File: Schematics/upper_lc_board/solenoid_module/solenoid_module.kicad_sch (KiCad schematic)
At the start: 10 parts, among them J1 SOL_CONN, K1 RELAY_G5Q-1A, Q1 MOSFET_IRLZ44N

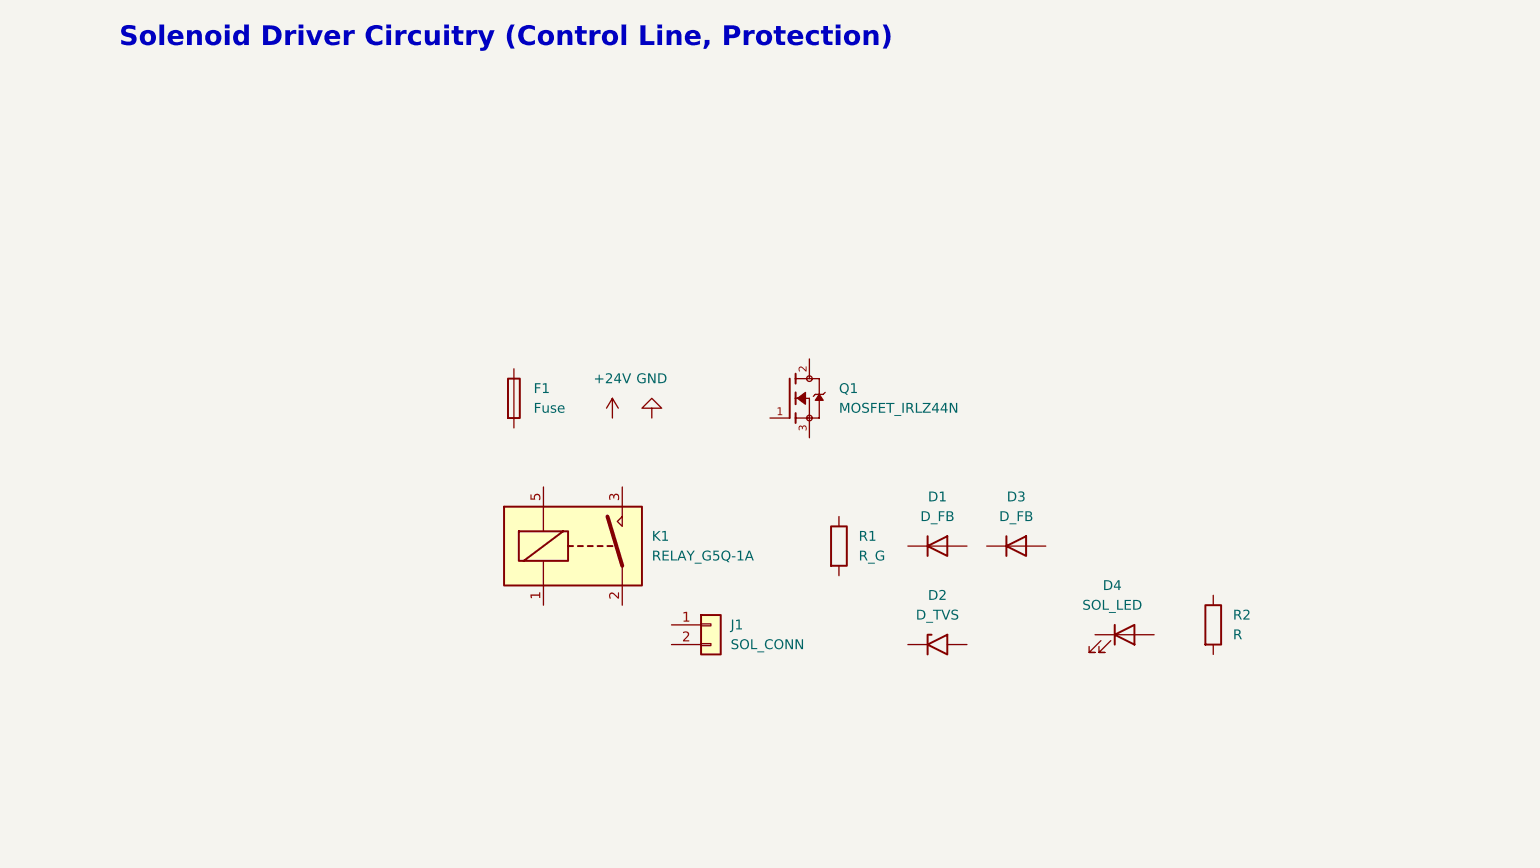
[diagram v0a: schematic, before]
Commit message: add solenoid driver circuitry
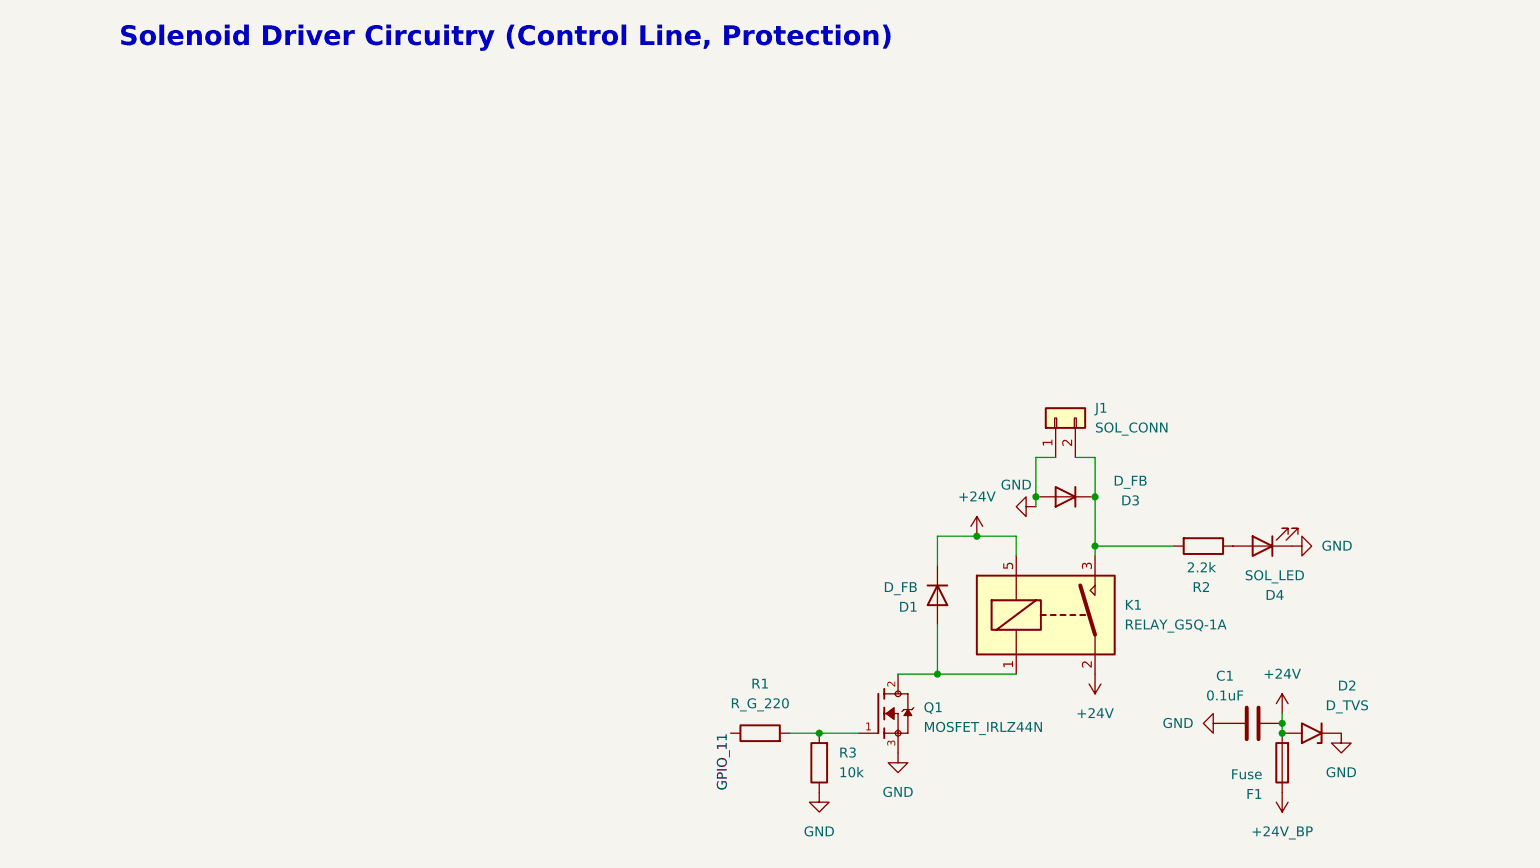
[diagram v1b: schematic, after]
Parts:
- added C1: 0.1uF, symbol Device:C
- added R3: 10k, symbol Device:R
- R1: value R_G -> R_G_220
- R2: value R -> 2.2k
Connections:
- net +24V: now also D1.1 (K), D2.2 (A2), F1.2, K1.2, K1.5, C1.2
- net GND: now also D2.1 (A1), D3.2 (A), D4.1 (K), J1.1 (Pin_1), Q1.3, C1.1, R3.1
- net GPIO_11: now reaches R1.1
- net at R1.2: now also Q1.1, R3.2
- net +24V_BP: now reaches F1.1
- net at R2.1: now also D4.2 (A)
- net at R2.2: now also D3.1 (K), J1.2 (Pin_2), K1.3
- net at D1.2 (A): now also K1.1, Q1.2
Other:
- moved on the sheet: F1, J1, K1, Q1, R1

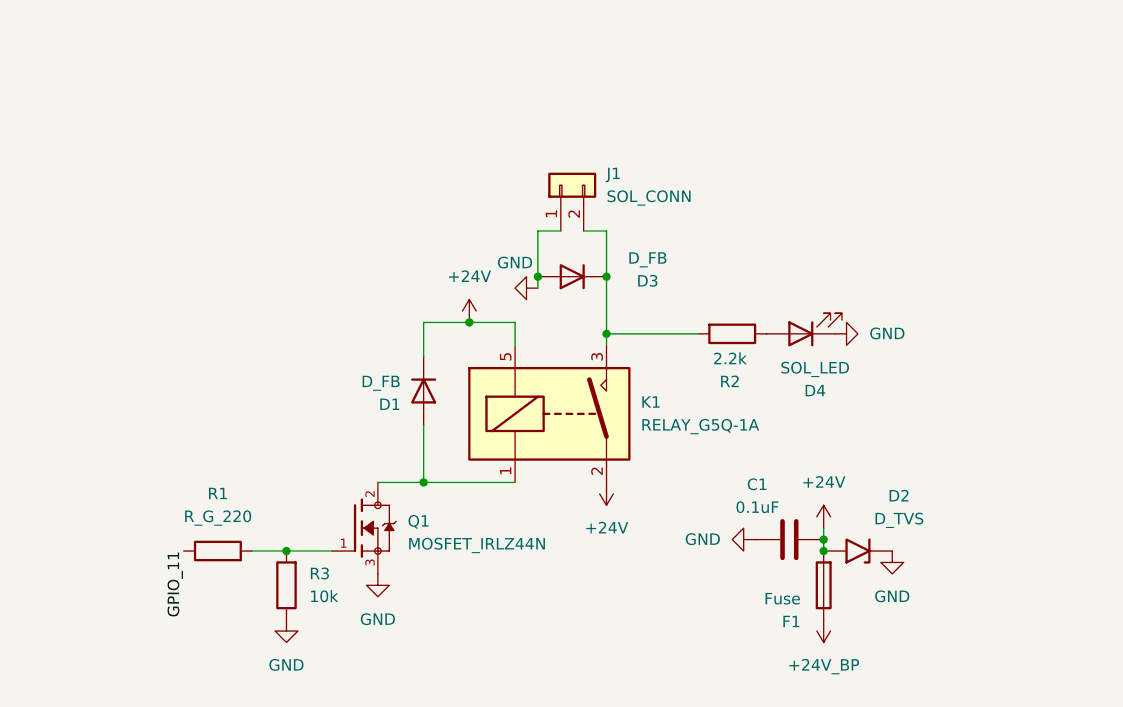
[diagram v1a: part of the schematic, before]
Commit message: SSR replacement for solenoid driver
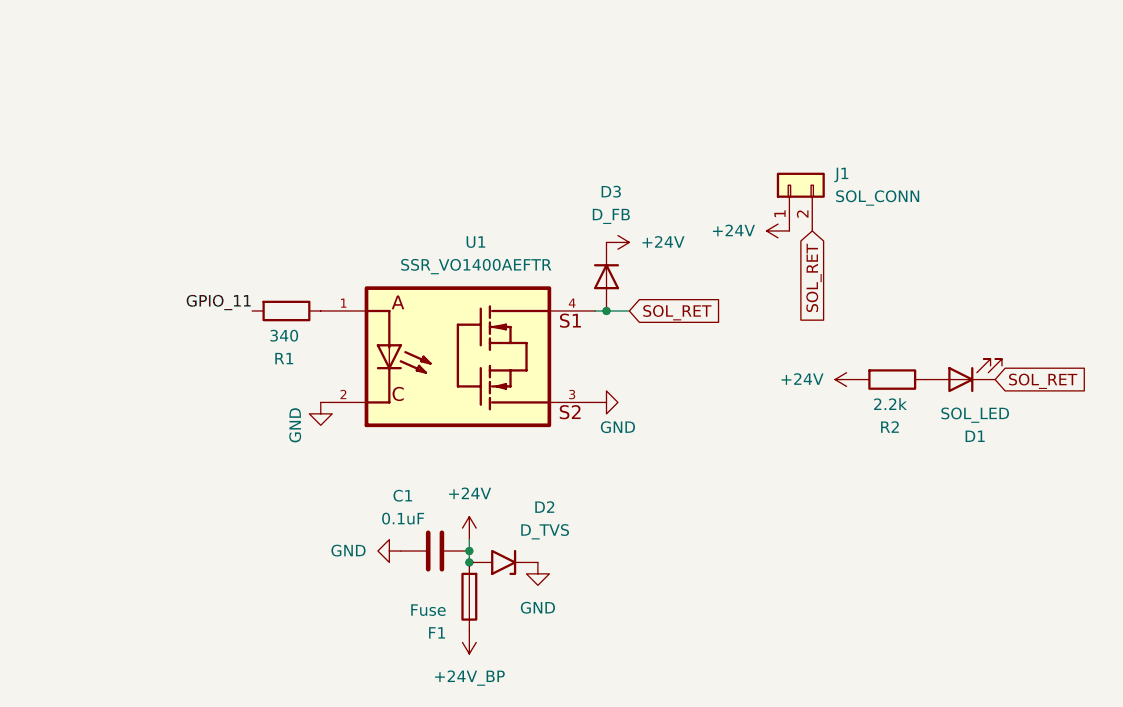
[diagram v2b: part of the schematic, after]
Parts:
- removed D1: D_FB, symbol Device:D
- removed D4: SOL_LED, symbol Device:LED
- removed K1: RELAY_G5Q-1A, Relay_THT:Relay_SPST_Omron-G5Q-1A, symbol Relay:G5Q-1A
- removed Q1: MOSFET_IRLZ44N, IRLZ44N:TO254P1054X469X1930-3, symbol IRLZ44N:IRLZ44N
- removed R3: 10k, symbol Device:R
- added D1: SOL_LED, symbol Device:LED
- added U1: SSR_VO1400AEFTR, VO1400AEFTR:SOIC254P695X242-4N, symbol VO1400AEFTR:VO1400AEFTR
- R1: value R_G_220 -> 340
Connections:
- net +24V: now also D3.1 (K), J1.1 (Pin_1), R2.2
- net GND: now also U1.2, U1.3; no longer D3.2 (A), J1.1 (Pin_1)
- net GPIO_11: now also R1.2; no longer R1.1
- net at R2.1: now also D1.2 (A)
- new net: R1.1, U1.1
- new net SOL_RET: D1.1 (K), D3.2 (A), J1.2 (Pin_2), U1.4
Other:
- moved on the sheet: C1, D2, F1, J1

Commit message: add hiearchical sheets in main board file
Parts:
- removed D3: D_FB, symbol Device:D
- added D3, D4: D_FB, symbol Device:D_Schottky
- added D5: SOL_LED, symbol Device:LED
- added J2: SOL2_CONN, symbol Connector_Generic:Conn_01x02
- added Q1: IRLZ44N, IRLZ44N:TO254P1054X469X1930-3, symbol IRLZ44N:IRLZ44N
- added R3: 340, symbol Device:R
- added R4: 100k, symbol Device:R
- added R5: 2.2k, symbol Device:R
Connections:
- net +24V: now also D3.1 (K), D4.1 (K), J2.1 (Pin_1), R5.2
- net GND: now also Q1.3, R4.1
- net SOL_RET: now also D5.1 (K); no longer J1.2 (Pin_2), U1.4
- new net: D5.2 (A), R5.1
- new net: Q1.1, R3.1, R4.2
- new net GPIO_12: R3.2
- new net SOL1_RET: D3.2 (A), J1.2 (Pin_2), U1.4
- new net SOL2_RET: D4.2 (A), J2.2 (Pin_2), Q1.2
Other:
- moved on the sheet: C1, D1, D2, F1, J1, R1, R2, U1

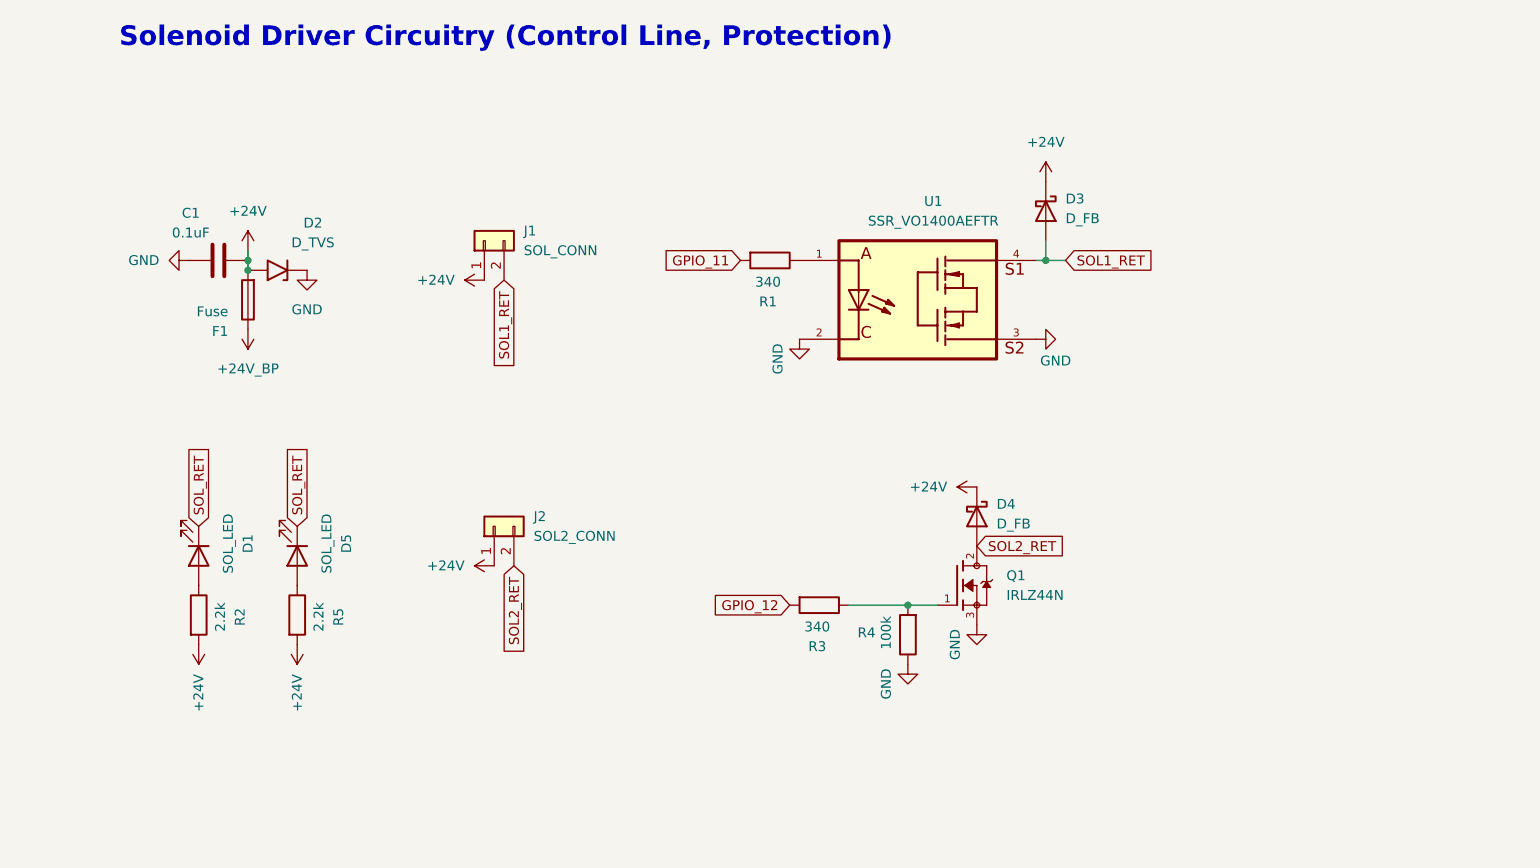
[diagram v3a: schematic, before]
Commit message: global symbols/component annotations fix
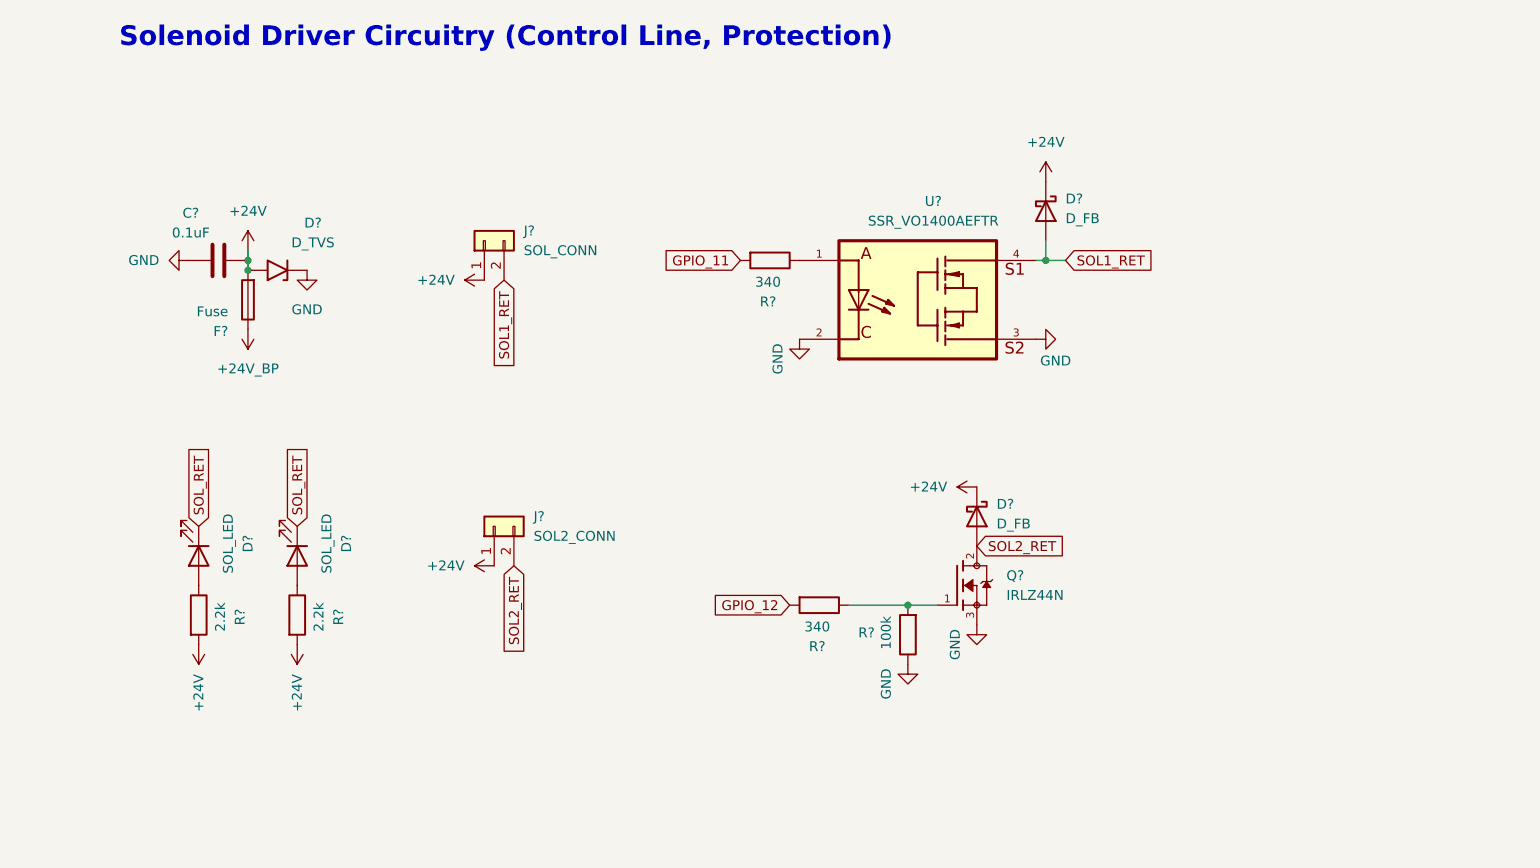
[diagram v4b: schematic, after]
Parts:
- renumbered C1 to C?, D5 to D?, D4 to D?, D2 to D?, D1 to D?, D3 to D?, F1 to F?, J1 to J?, J2 to J?, Q1 to Q?, R1 to R?, R2 to R?, R4 to R?, R3 to R?, R5 to R?, U1 to U?

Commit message: start PCB file, start assigning footprints, omit fuse, JST conns for now, still assigning resistors and some diodes
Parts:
- C?: footprint (none) -> Capacitor_SMD:C_0603_1608Metric
- J? (x2): footprint (none) -> Connector_JST:JST_EH_S2B-EH_1x02_P2.50mm_Horizontal
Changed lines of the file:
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@@
 			)
 		)
-		(property "Footprint" ""
+		(property "Footprint" "Capacitor_SMD:C_0603_1608Metric"
 			(at 31.75 49.8348 0)
 			(effects
@@
 			)
 		)
-		(property "Footprint" ""
+		(property "Footprint" "Connector_JST:JST_EH_S2B-EH_1x02_P2.50mm_Horizontal"
 			(at 62.23 48.26 0)
 			(effects
@@
 			)
 		)
-		(property "Footprint" ""
+		(property "Footprint" "Connector_JST:JST_EH_S2B-EH_1x02_P2.50mm_Horizontal"
 			(at 63.5 85.09 0)
 			(effects

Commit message: start layout, finish assigning footprints. TODO -> verify ESP32 pinout, continue layout
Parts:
- D? (x2): footprint (none) -> LED_SMD:LED_1206_3216Metric
- D? (x2): footprint (none) -> US1M:DIOM4325X250N
- R? (x3): footprint (none) -> Resistor_SMD:R_0603_1608Metric
- R? (x2): footprint (none) -> Resistor_SMD:R_1210_3225Metric
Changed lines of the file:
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@@
 			)
 		)
-		(property "Footprint" ""
+		(property "Footprint" "LED_SMD:LED_1206_3216Metric"
 			(at 38.1 88.9 0)
 			(effects
@@
 			)
 		)
-		(property "Footprint" ""
+		(property "Footprint" "Resistor_SMD:R_0603_1608Metric"
 			(at 99.06 49.022 90)
 			(effects
@@
 			)
 		)
-		(property "Footprint" ""
+		(property "Footprint" "US1M:DIOM4325X250N"
 			(at 125.73 83.82 0)
 			(effects
@@
 			)
 		)
-		(property "Datasheet" "https://www.mccsemi.com/pdf/Products/SK42BL-SK44BL(DO-214AA).pdf"
+		(property "Datasheet" "https://services.taiwansemi.com/storage/resources/datasheet/US1A%20SERIES_N2102.pdf"
 			(at 125.73 83.82 0)
 			(effects
@@
 			)
 		)
-		(property "Description" "Schottky diode for flyback"
+		(property "Description" "Schottky diode for flyback, UPDATED to USM (safer/larger VRRM)"
 			(at 125.73 83.82 0)
 			(effects
@@
 			)
 		)
-		(property "Footprint" ""
+		(property "Footprint" "Resistor_SMD:R_1210_3225Metric"
 			(at 23.622 96.52 90)
 			(effects
@@
 			)
 		)
-		(property "Footprint" ""
+		(property "Footprint" "Resistor_SMD:R_0603_1608Metric"
 			(at 118.618 99.06 90)
 			(effects
@@
 			)
 		)
-		(property "Footprint" ""
+		(property "Footprint" "Resistor_SMD:R_0603_1608Metric"
 			(at 105.41 93.472 90)
 			(effects
@@
 			)
 		)
-		(property "Footprint" ""
+		(property "Footprint" "Resistor_SMD:R_1210_3225Metric"
 			(at 36.322 96.52 90)
 			(effects
@@
 			)
 		)
-		(property "Footprint" ""
+		(property "Footprint" "LED_SMD:LED_1206_3216Metric"
 			(at 25.4 88.9 0)
 			(effects
@@
 			)
 		)
-		(property "Footprint" ""
+		(property "Footprint" "US1M:DIOM4325X250N"
 			(at 134.62 44.45 0)
 			(effects

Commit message: layout update; still need to add small components (caps, resistors), and add silkscreen
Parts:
- Q?: footprint IRLZ44N:TO254P1054X469X1930-3 -> IRFZ44NSPBF:TO254P1524X483-4N
- R? (x3): footprint Resistor_SMD:R_0603_1608Metric -> Capacitor_SMD:C_0402_1005Metric
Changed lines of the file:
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@@
 			)
 		)
-		(property "Footprint" "IRLZ44N:TO254P1054X469X1930-3"
+		(property "Footprint" "IRFZ44NSPBF:TO254P1524X483-4N"
 			(at 123.19 92.71 0)
 			(effects
@@
 			)
 		)
-		(property "Footprint" "Resistor_SMD:R_0603_1608Metric"
+		(property "Footprint" "Capacitor_SMD:C_0402_1005Metric"
 			(at 99.06 49.022 90)
 			(effects
@@
 			)
 		)
-		(property "Footprint" "Resistor_SMD:R_0603_1608Metric"
+		(property "Footprint" "Capacitor_SMD:C_0402_1005Metric"
 			(at 118.618 99.06 90)
 			(effects
@@
 			)
 		)
-		(property "Footprint" "Resistor_SMD:R_0603_1608Metric"
+		(property "Footprint" "Capacitor_SMD:C_0402_1005Metric"
 			(at 105.41 93.472 90)
 			(effects

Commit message: small
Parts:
- D? (x2): footprint LED_SMD:LED_1206_3216Metric -> LED_SMD:LED_0805_2012Metric
- D? (x2): footprint US1M:DIOM4325X250N -> SK44BL-TP:DIOM4336X265N
- D?: footprint Diode_THT:D_DO-201AE_P15.24mm_Horizontal -> SMBJ28A:DIOM5436X244N
- Q?: value IRLZ44N -> MOSFET_BSS138; footprint IRFZ44NSPBF:TO254P1524X483-4N -> BSS138:SOT95P240X111-3N
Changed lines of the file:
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@@
 			)
 		)
-		(property "Footprint" "LED_SMD:LED_1206_3216Metric"
+		(property "Footprint" "LED_SMD:LED_0805_2012Metric"
 			(at 38.1 88.9 0)
 			(effects
@@
 			)
 		)
-		(property "Value" "IRLZ44N"
+		(property "Value" "MOSFET_BSS138"
 			(at 129.54 93.9799 0)
 			(effects
@@
 			)
 		)
-		(property "Footprint" "IRFZ44NSPBF:TO254P1524X483-4N"
+		(property "Footprint" "BSS138:SOT95P240X111-3N"
 			(at 123.19 92.71 0)
 			(effects
@@
 			)
 		)
-		(property "Datasheet" ""
+		(property "Datasheet" "https://www.onsemi.com/pdf/datasheet/bss138-d.pdf"
 			(at 123.19 92.71 0)
 			(effects
@@
 			)
 		)
-		(property "Footprint" "US1M:DIOM4325X250N"
+		(property "Footprint" "SK44BL-TP:DIOM4336X265N"
 			(at 125.73 83.82 0)
 			(effects
@@
 			)
 		)
-		(property "Datasheet" "https://services.taiwansemi.com/storage/resources/datasheet/US1A%20SERIES_N2102.pdf"
+		(property "Datasheet" "https://www.mccsemi.com/pdf/Products/SK42BL-SK44BL(DO-214AA).pdf"
 			(at 125.73 83.82 0)
 			(effects
@@
 			)
 		)
-		(property "Description" "Schottky diode for flyback, UPDATED to USM (safer/larger VRRM)"
+		(property "Description" "Schottky diode for flyback"
 			(at 125.73 83.82 0)
 			(effects
@@
 			)
 		)
-		(property "Footprint" "Diode_THT:D_DO-201AE_P15.24mm_Horizontal"
+		(property "Footprint" "SMBJ28A:DIOM5436X244N"
 			(at 35.56 46.99 0)
 			(effects
@@
 			)
 		)
-		(property "Datasheet" "https://www.vishay.com/docs/88301/15ke.pdf"
+		(property "Datasheet" "https://www.littelfuse.com/assetdocs/tvs-diodes-smbj-series-datasheet?assetguid=ba555e99-a12d-4f72-a0b6-86b06c67171e"
 			(at 36.83 52.07 0)
 			(effects
@@
 			)
 		)
-		(property "Footprint" "LED_SMD:LED_1206_3216Metric"
+		(property "Footprint" "LED_SMD:LED_0805_2012Metric"
 			(at 25.4 88.9 0)
 			(effects
@@
 			)
 		)
-		(property "Footprint" "US1M:DIOM4325X250N"
+		(property "Footprint" "SK44BL-TP:DIOM4336X265N"
 			(at 134.62 44.45 0)
 			(effects
@@
 			)
 		)
-		(property "Description" "Schottky diode for flyback"
+		(property "Description" "SK44BL-TP Schottky diode for flyback"
 			(at 134.62 44.45 0)
 			(effects
